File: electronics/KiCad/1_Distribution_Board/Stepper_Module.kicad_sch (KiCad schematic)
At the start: 18 parts, among them J1 Jumper Pins, J2 Jumper Pins, J3 JST PH, J4 Generic 2.54mm, J5 Conn_01x08_Socket, J6 Conn_01x02_Socket, J7 Conn_01x08_Socket

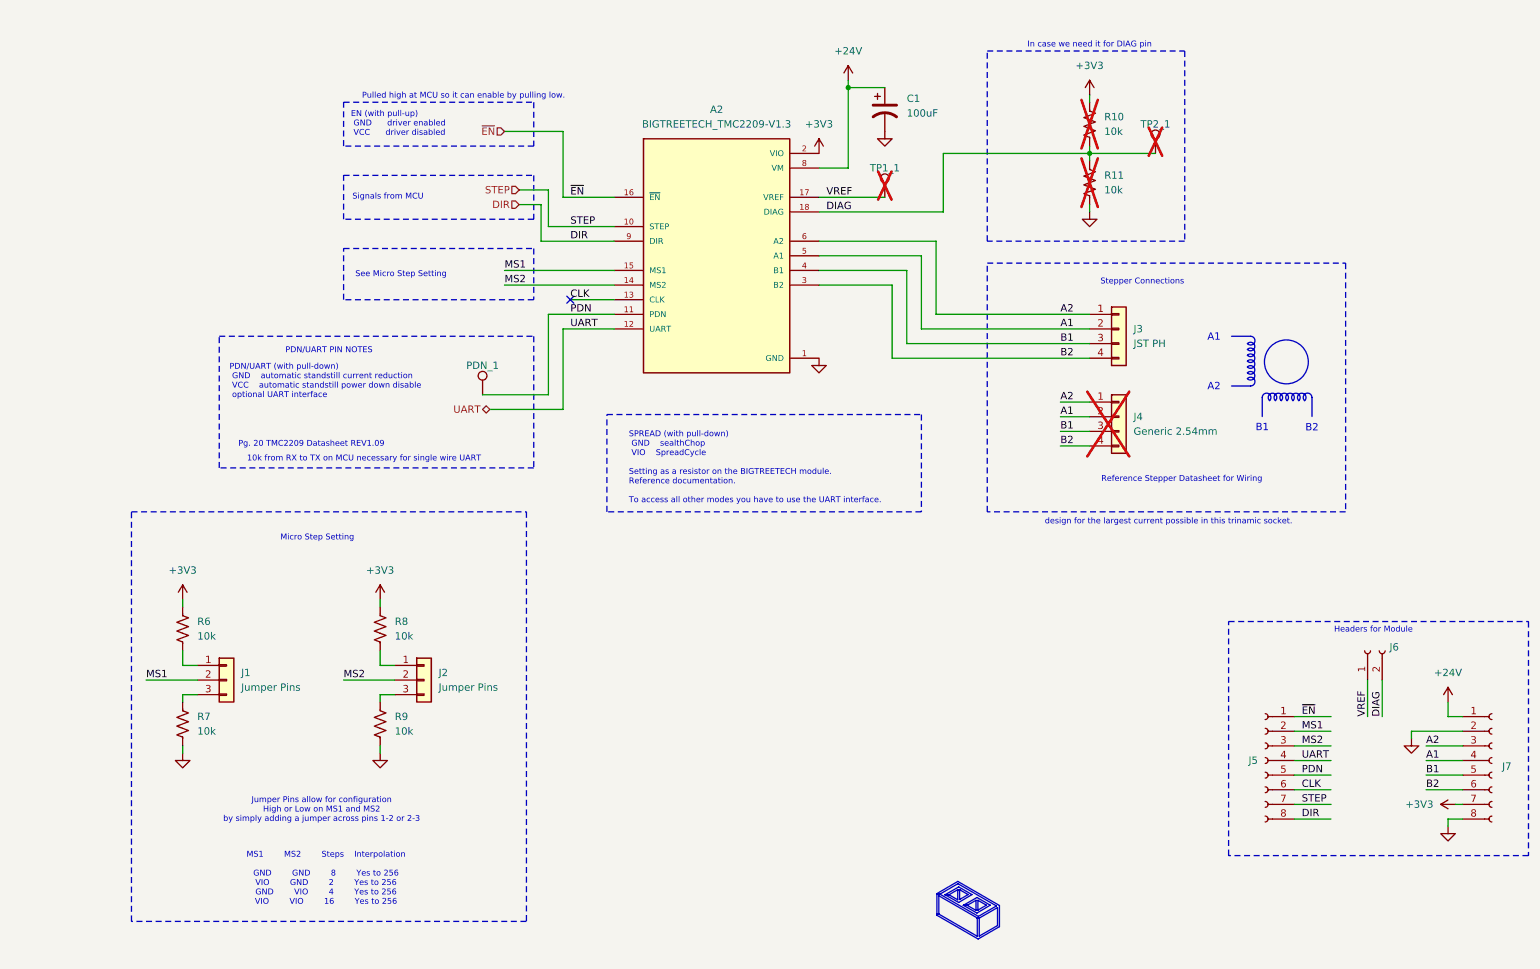
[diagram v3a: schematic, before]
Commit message: Additional Routing and placement
Updated power page on schematic to remove redundant connections. Removed test points on steppers since the steppers drivers chosen have test points on them. Updated placement and cleaned up silk. Started placing final power connections.
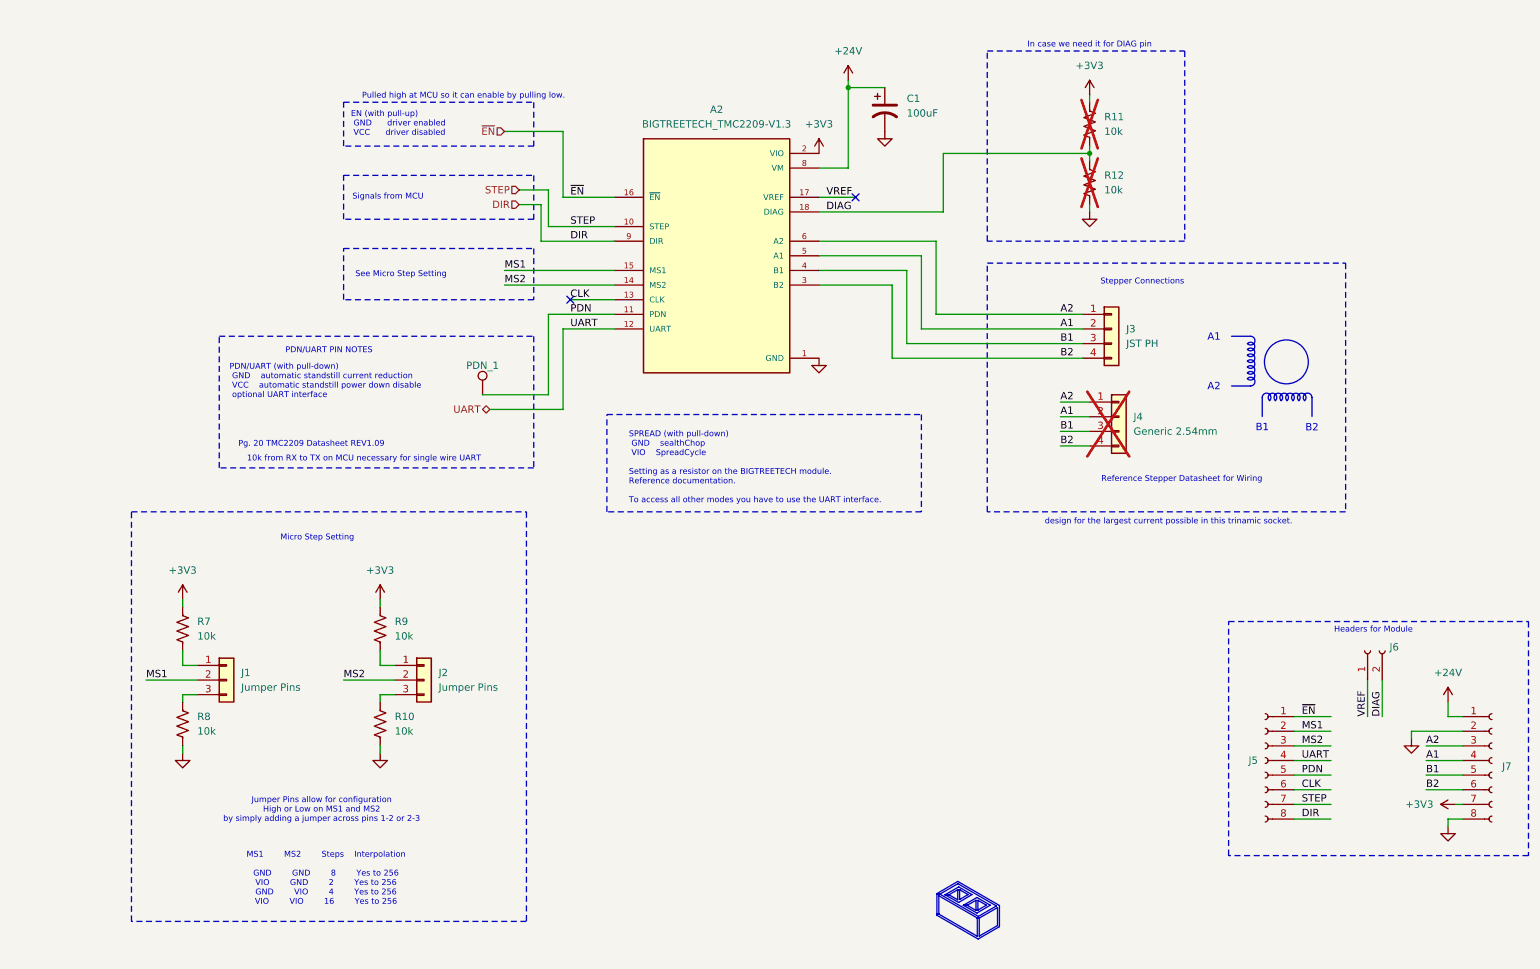
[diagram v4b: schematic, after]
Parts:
- removed TP1_1, TP2_1: PTH, Connector_PinHeader_2.54mm:PinHeader_1x01_P2.54mm_Vertical, symbol PCM_SparkFun-Connector:TestPoint_PTH
- renumbered R9 to R10, R10 to R11, R11 to R12, R6 to R7, R7 to R8, R8 to R9
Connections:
- no-connect marks 1 -> 2
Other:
- moved on the sheet: J3

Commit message: Mid work update
Lots of rework on the SCH and PCB. Checkpoint.
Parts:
- removed J5, J7: Conn_01x08_Socket, Connector_PinSocket_2.54mm:PinSocket_1x08_P2.54mm_Vertical, symbol Connector:Conn_01x08_Socket
- removed J6: Conn_01x02_Socket, Connector_PinSocket_2.54mm:PinSocket_1x02_P2.54mm_Vertical, symbol Connector:Conn_01x02_Socket
- removed R10, R7, R8, R9: 10k, Resistor_SMD:R_0805_2012Metric_Pad1.20x1.40mm_HandSolder, symbol Device:R_US
- added J25, J27: Header-Female-2.54_1x8, Connector_PinSocket_2.54mm:PinSocket_1x08_P2.54mm_Vertical, symbol EasyEDA:Header-Female-2.54_1x8
- added P1: Header-Female-2.54_1x2, Connector_PinSocket_2.54mm:PinSocket_1x02_P2.54mm_Vertical, symbol EasyEDA:Header-Female-2.54_1x2
- added R69, R70, R71, R72: 10kΩ, PCM_JLCPCB:R_0603, symbol PCM_JLCPCB-Resistors:0603,10kΩ
- J22: renamed from J1; LCSC Part (none) -> C49257
- J23: renamed from J2; LCSC Part (none) -> C49257
- J24: renamed from J3; LCSC Part (none) -> C566011
- J26: renamed from J4; LCSC Part (none) -> C2691448
- renumbered C1 to C15, R11 to R73, R12 to R74
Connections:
- net +24V: now also J27.1
- net +3V3: now also J27.7, R69.1, R71.1
- net A1: now also J27.4
- net A2: now also J27.3
- net B1: now also J27.5
- net B2: now also J27.6
- net CLK: now also J25.6
- net DIAG: now also P1.2
- net DIR: now also J25.8
- net GND: now also J27.2, J27.8, R70.2, R72.2
- net MS1: now also J25.2
- net MS2: now also J25.3
- net PDN: now also J25.5
- net STEP: now also J25.7
- net UART: now also J25.4
- net VREF: now also P1.1
- net ~{EN}: now also J25.1
- net at J23.1 (Pin_1): now also R71.2
- net at J23.3 (Pin_3): now also R72.1
- net at J22.1 (Pin_1): now also R69.2
- net at J22.3 (Pin_3): now also R70.1
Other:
- note added: "Requires 2 Jumpers JLCPCB # C5305"

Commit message: Updated with more layout
Compelted PCA on board.
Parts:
- C15: footprint Capacitor_THT:CP_Radial_D8.0mm_P2.50mm -> EasyEDA:CAP-SMD_BD6.3-L6.6-W6.6-LS7.4-FD; LCSC (none) -> C2836442
- J24: LCSC Part C566011 -> C131334
- J26: now fitted
- renumbered J27 to P2
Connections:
- net A1: no longer P2.4
- net A2: no longer P2.3
- net B1: no longer P2.5
- net B2: no longer P2.6
- new net A_1: P2.4
- new net A_2: P2.3
- new net B_1: P2.5
- new net B_2: P2.6
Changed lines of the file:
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@@
 		)
 	)
-	(label "B1"
+	(label "B_1"
 		(at 232.41 148.59 0)
 		(effects
@@
 		)
 	)
-	(label "B2"
+	(label "B_2"
 		(at 232.41 151.13 0)
 		(effects
@@
 		)
 	)
-	(label "A2"
+	(label "A_2"
 		(at 232.41 143.51 0)
 		(effects
@@
 		)
 	)
-	(label "A1"
+	(label "A_1"
 		(at 232.41 146.05 0)
 		(effects
@@
 				)
 				(path "/d53c8c01-e754-4310-8a73-7d7c95e64cd3/7a480abb-9b9a-47ac-a44b-24d5185d46e0"
-					(reference "J29")
+					(reference "J28")
 					(unit 1)
 				)
 				(path "/d53c8c01-e754-4310-8a73-7d7c95e64cd3/be0591dd-6b80-4d9a-a31b-18ff19c250bb"
-					(reference "J39")
+					(reference "J36")
 					(unit 1)
 				)
 				(path "/d53c8c01-e754-4310-8a73-7d7c95e64cd3/ec0756a4-872d-4fc6-b758-9ad2624703a8"
-					(reference "J34")
+					(reference "J32")
 					(unit 1)
 				)
@@
 			)
 		)
-		(property "LCSC Part" "C566011"
+		(property "LCSC Part" "C131334"
 			(at 209.55 71.12 0)
 			(effects
@@
 				)
 				(path "/d53c8c01-e754-4310-8a73-7d7c95e64cd3/7a480abb-9b9a-47ac-a44b-24d5185d46e0"
-					(reference "J30")
+					(reference "J29")
 					(unit 1)
 				)
 				(path "/d53c8c01-e754-4310-8a73-7d7c95e64cd3/be0591dd-6b80-4d9a-a31b-18ff19c250bb"
-					(reference "J40")
+					(reference "J37")
 					(unit 1)
 				)
 				(path "/d53c8c01-e754-4310-8a73-7d7c95e64cd3/ec0756a4-872d-4fc6-b758-9ad2624703a8"
-					(reference "J35")
+					(reference "J33")
 					(unit 1)
 				)
@@
 		(in_bom yes)
 		(on_board yes)
-		(dnp yes)
+		(dnp no)
 		(fields_autoplaced yes)
 		(property "Reference" "J26"
@@
 				)
 				(path "/d53c8c01-e754-4310-8a73-7d7c95e64cd3/7a480abb-9b9a-47ac-a44b-24d5185d46e0"
-					(reference "J31")
+					(reference "J30")
 					(unit 1)
 				)
 				(path "/d53c8c01-e754-4310-8a73-7d7c95e64cd3/be0591dd-6b80-4d9a-a31b-18ff19c250bb"
-					(reference "J41")
+					(reference "J38")
 					(unit 1)
 				)
 				(path "/d53c8c01-e754-4310-8a73-7d7c95e64cd3/ec0756a4-872d-4fc6-b758-9ad2624703a8"
-					(reference "J36")
+					(reference "J34")
 					(unit 1)
 				)
@@
 				)
 				(path "/d53c8c01-e754-4310-8a73-7d7c95e64cd3/7a480abb-9b9a-47ac-a44b-24d5185d46e0"
-					(reference "P2")
+					(reference "P3")
 					(unit 1)
 				)
 				(path "/d53c8c01-e754-4310-8a73-7d7c95e64cd3/be0591dd-6b80-4d9a-a31b-18ff19c250bb"
-					(reference "P6")
+					(reference "P9")
 					(unit 1)
 				)
 				(path "/d53c8c01-e754-4310-8a73-7d7c95e64cd3/ec0756a4-872d-4fc6-b758-9ad2624703a8"
-					(reference "P4")
+					(reference "P6")
 					(unit 1)
 				)
@@
 		(on_board yes)
 		(dnp no)
-		(property "Reference" "J27"
+		(property "Reference" "P2"
 			(at 247.65 146.0499 0)
 			(effects
@@
 			(project "1_Distribution_Board"
 				(path "/d53c8c01-e754-4310-8a73-7d7c95e64cd3/02dc68e7-469d-4169-b9e6-1742ced64b14"
-					(reference "J27")
+					(reference "P2")
 					(unit 1)
 				)
 				(path "/d53c8c01-e754-4310-8a73-7d7c95e64cd3/7a480abb-9b9a-47ac-a44b-24d5185d46e0"
-					(reference "J32")
+					(reference "P5")
 					(unit 1)
 				)
 				(path "/d53c8c01-e754-4310-8a73-7d7c95e64cd3/be0591dd-6b80-4d9a-a31b-18ff19c250bb"
-					(reference "J42")
+					(reference "P11")
 					(unit 1)
 				)
 				(path "/d53c8c01-e754-4310-8a73-7d7c95e64cd3/ec0756a4-872d-4fc6-b758-9ad2624703a8"
-					(reference "J37")
+					(reference "P8")
 					(unit 1)
 				)
@@
 				)
 				(path "/d53c8c01-e754-4310-8a73-7d7c95e64cd3/7a480abb-9b9a-47ac-a44b-24d5185d46e0"
-					(reference "P3")
+					(reference "P4")
 					(unit 1)
 				)
 				(path "/d53c8c01-e754-4310-8a73-7d7c95e64cd3/be0591dd-6b80-4d9a-a31b-18ff19c250bb"
-					(reference "P7")
+					(reference "P10")
 					(unit 1)
 				)
 				(path "/d53c8c01-e754-4310-8a73-7d7c95e64cd3/ec0756a4-872d-4fc6-b758-9ad2624703a8"
-					(reference "P5")
+					(reference "P7")
 					(unit 1)
 				)
@@
 			)
 		)
-		(property "Footprint" "Capacitor_THT:CP_Radial_D8.0mm_P2.50mm"
+		(property "Footprint" "EasyEDA:CAP-SMD_BD6.3-L6.6-W6.6-LS7.4-FD"
 			(at 170.18 33.02 0)
 			(effects
@@
 			)
 		)
+		(property "LCSC" "C2836442"
+			(at 170.18 33.02 0)
+			(effects
+				(font
+					(size 1.27 1.27)
+				)
+				(hide yes)
+			)
+		)
 		(pin "1"
 		)
@@
 				)
 				(path "/d53c8c01-e754-4310-8a73-7d7c95e64cd3/7a480abb-9b9a-47ac-a44b-24d5185d46e0"
-					(reference "J28")
+					(reference "J27")
 					(unit 1)
 				)
 				(path "/d53c8c01-e754-4310-8a73-7d7c95e64cd3/be0591dd-6b80-4d9a-a31b-18ff19c250bb"
-					(reference "J38")
+					(reference "J35")
 					(unit 1)
 				)
 				(path "/d53c8c01-e754-4310-8a73-7d7c95e64cd3/ec0756a4-872d-4fc6-b758-9ad2624703a8"
-					(reference "J33")
+					(reference "J31")
 					(unit 1)
 				)

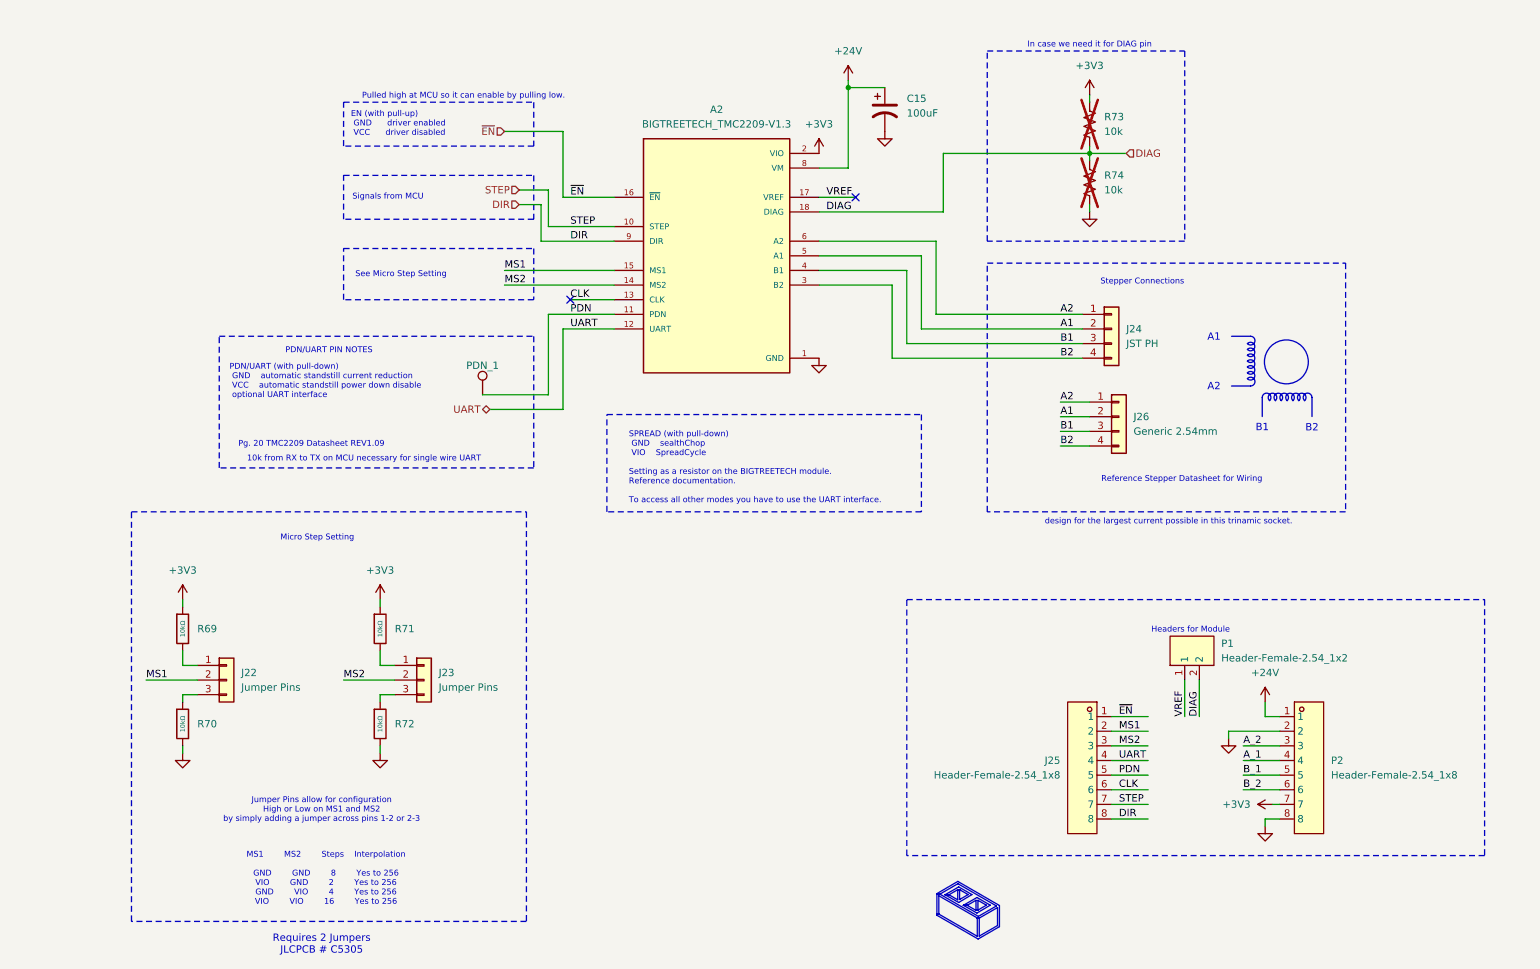
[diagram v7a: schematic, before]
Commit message: REV0.9 for review
Took care of all open items on the electronics PCB except for the driver resistor addresses.
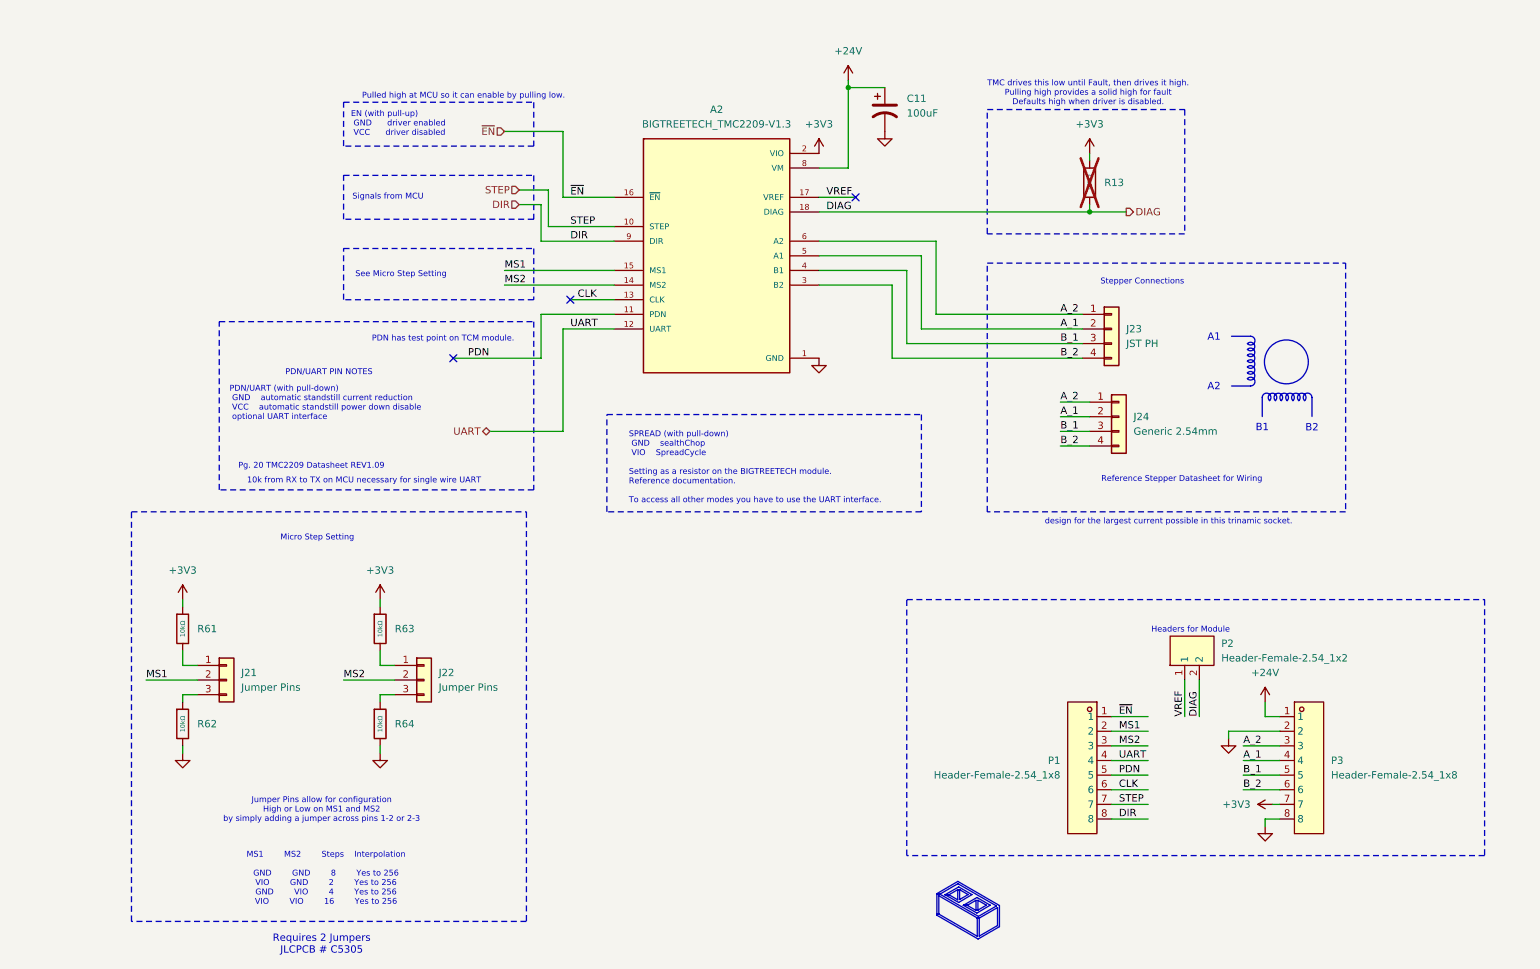
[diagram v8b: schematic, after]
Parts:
- removed PDN_1: PTH, Connector_PinHeader_2.54mm:PinHeader_1x01_P2.54mm_Vertical, symbol PCM_SparkFun-Connector:TestPoint_PTH
- removed R73, R74: 10k, Resistor_SMD:R_0805_2012Metric_Pad1.20x1.40mm_HandSolder, symbol Device:R_US
- added R13: 10kΩ, PCM_JLCPCB:R_0603, symbol PCM_JLCPCB-Resistors:0603,10kΩ
- renumbered C15 to C11, J22 to J21, J23 to J22, J24 to J23, J26 to J24, J25 to P1, P1 to P2, P2 to P3, R69 to R61, R70 to R62, R71 to R63, R72 to R64
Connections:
- net A1 is gone; now on net A_1: A2.5 (A1), J23.2 (Pin_2), J24.2 (Pin_2)
- net A2 is gone; now on net A_2: A2.6 (A2), J23.1 (Pin_1), J24.1 (Pin_1)
- net B1 is gone; now on net B_1: A2.4 (B1), J23.3 (Pin_3), J24.3 (Pin_3)
- net B2 is gone; now on net B_2: A2.3 (B2), J23.4 (Pin_4), J24.4 (Pin_4)
- net +3V3: now also R13.1
- net DIAG: now also R13.2
- no-connect marks 2 -> 3
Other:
- note added: "PDN has test point on TCM module."
- note added: "TMC drives this low until Fault, then drives it high. Pulling high provides a solid high for fault Defaults high when driver is disabled."
- note removed: "In case we need it for DIAG pin"
